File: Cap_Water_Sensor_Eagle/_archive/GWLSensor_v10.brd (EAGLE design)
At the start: 12 parts

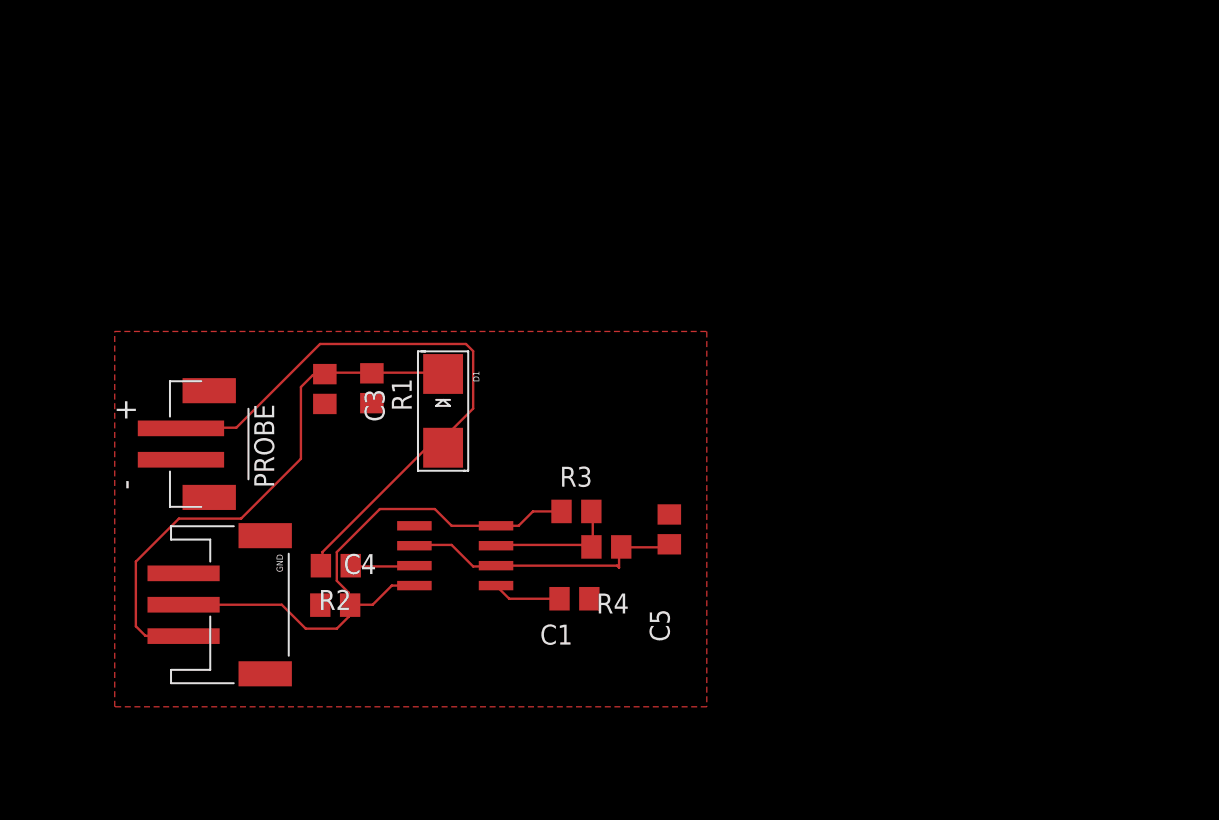
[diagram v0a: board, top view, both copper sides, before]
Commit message: Change3d to new name and added board parts
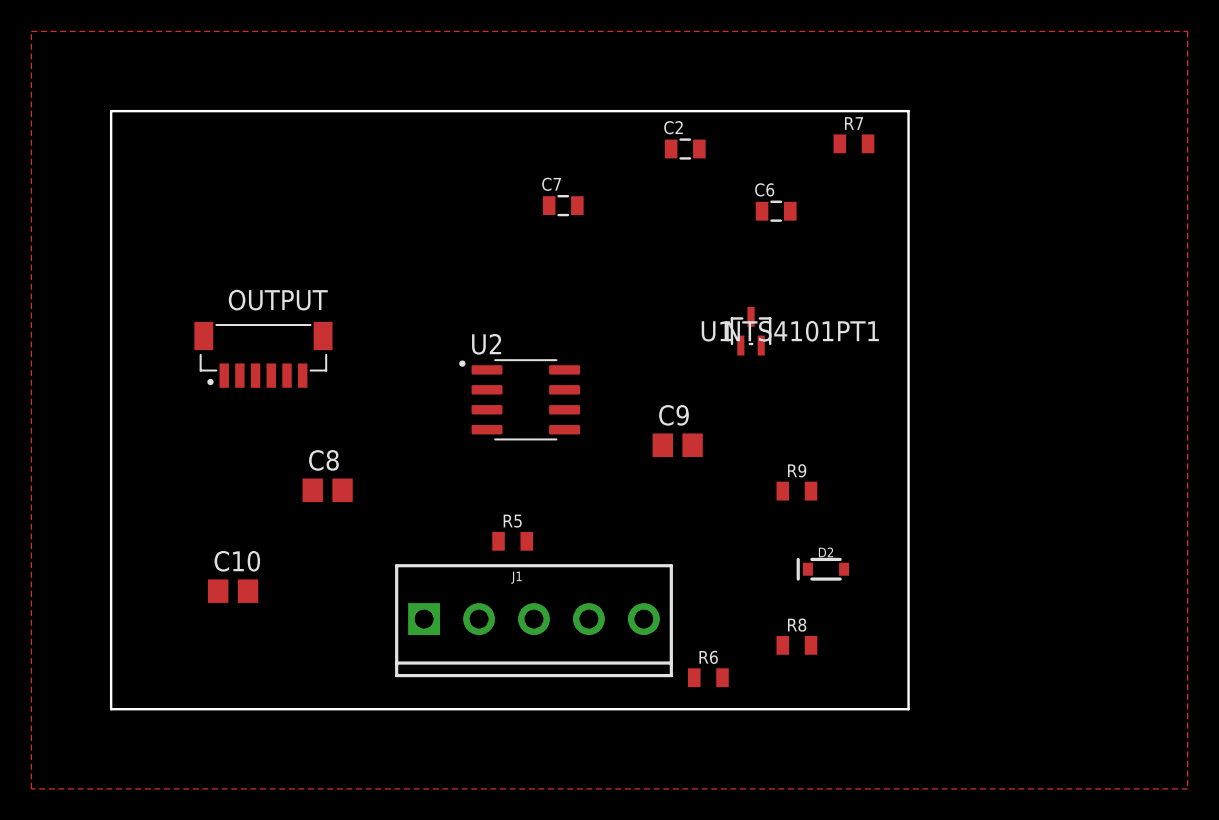
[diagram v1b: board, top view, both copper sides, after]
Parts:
- removed 555: LM555D, linear:SO08
- removed C1: 10nf, rcl:C0805
- removed C3: 1n, rcl:C0805
- removed C4: 100nf, rcl:C0805
- removed C5: 470pf, rcl:C0805
- removed D1: (no value), adafruit:SMADIODE
- removed GND: (no value), adafruit:JSTPH3
- removed PROBE: (no value), adafruit:JST-PH-2-SMT
- removed R1: 1M, rcl:R0805
- removed R2: 10K, rcl:R0805
- removed R3: 330, rcl:R0805
- removed R4: 1K6, rcl:R0805
- added C10: 1uF, rcl:C0805
- added C2: 1uF, Custom Components:0805@1
- added C6: 10nF, Custom Components:0805@1
- added C7: 0.1uF, Custom Components:0805@1
- added C8: 10nf, rcl:C0805
- added C9: 470pf, rcl:C0805
- added D2: 250mA/100V, Custom Components:SOD-323
- added J1: (no value), SparkFun-Connectors:SCREWTERMINAL-3.5MM-5
- added OUTPUT: BM06B-SRSS-TBT(LF)(SN), Custom Components:JST_BM06B-SRSS-TB(LF)(SN)
- added R5: 10k, Custom Components:0805
- added R6: 1k, Custom Components:0805
- added R7: 100k, Custom Components:0805
- added R8: 330, Custom Components:0805
- added R9: 1M, Custom Components:0805
- added U1: NTS4101PT1, Custom Components:SOT_101PT1_ONS
- added U2: TLC555CD, Custom Components:SOIC127P599X175-8N
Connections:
- removed net N$2: 555.7, R3.2, R4.1
- removed net N$3: 555.2, 555.6, C5.1, R4.2
- removed net N$4: 555.5, C1.2
- removed net N$6: D1.A, PROBE.1, R2.1
- removed net N$7: 555.3, R2.2
- removed net SIGNAL: C3.1, D1.C, GND.3, R1.1
- new net !EN: OUTPUT.3, R7.1, U1.1
- new net +3V3: OUTPUT.2, R7.2, U1.2
- new net N$1: C8.2, U2.5
- new net N$5: R5.1, U2.3
- new net N$8: C9.2, R6.1, U2.2, U2.6
- new net N$9: R6.2, R8.1, U2.7
- new net NC: OUTPUT.6
- new net OUTPUT1: C10.2, D2.C, OUTPUT.4, R9.2
- new net OUTPUT2: OUTPUT.5
- new net SENSOR1: D2.A, J1.4, R5.2
- new net SENSOR2: J1.5
- new net SHEILD: J1.3
- net GND: now also C10.1, C2.2, C6.2, C7.2, C8.1, C9.1, J1.1, OUTPUT.1, OUTPUT.S1, OUTPUT.S2, R9.1, U2.1; no longer 555.1, C1.1, C3.2, C4.1, C5.2, GND.1, PROBE.2, R1.2
- net VCC: now also C2.1, C6.1, C7.1, J1.2, R8.2, U1.3, U2.4, U2.8; no longer 555.4, 555.8, C4.2, GND.2, R3.1
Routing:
- net N$6: track 39.4 -> 0.00 mm
- net VCC: track 36.9 -> 0.00 mm
- net SIGNAL: track 34.8 -> 0.00 mm
- net N$3: track 18.4 -> 0.00 mm
- net N$2: track 8.55 -> 0.00 mm
- net N$4: track 4.39 -> 0.00 mm
- net N$7: track 4.10 -> 0.00 mm
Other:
- board outline added: 50.8 x 38.1 mm
